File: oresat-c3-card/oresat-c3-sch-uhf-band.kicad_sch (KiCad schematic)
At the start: 124 parts, among them Q3 DMP2035UQ-7, Q4 DMN3028LQ-7, U18 LT5534, U19 BDCN-20-13+, U20 QPC1022, U21 TQP7M9105, U22 LT5534, U25 SN74LVC1G11IDCKRQ1, U26 TLV7041DBV, U27 SN74LVC1G04DCKR, U29 TQP3M9036, U32 SF2446E, U33 SF2446E, U40 MAX941EUA+, U44 AT86RF215, U45 NCS2-62+, U47 QPC1022, X3 TXETALSANF-26.000000

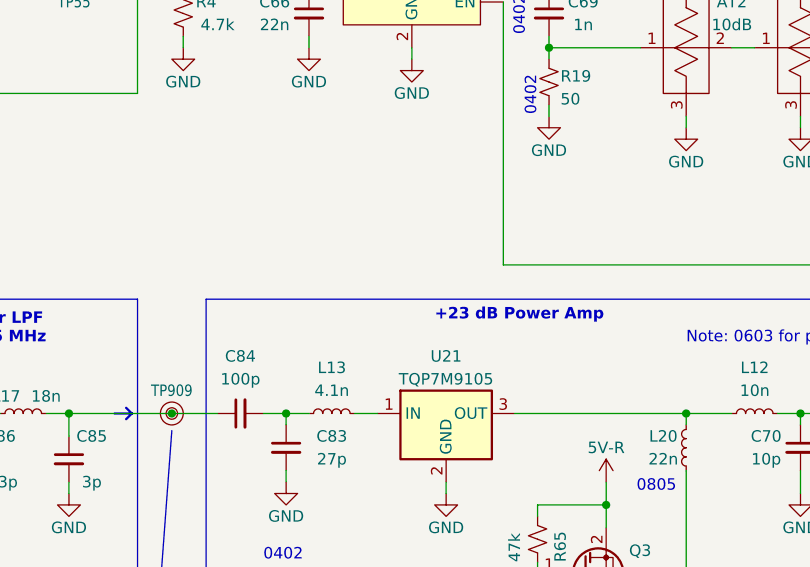
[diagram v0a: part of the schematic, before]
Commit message: All DRC exclusing RF traces are cleaned up.  RF traces cleaned up with mask and bends. Some more notes in the schematic for future us.
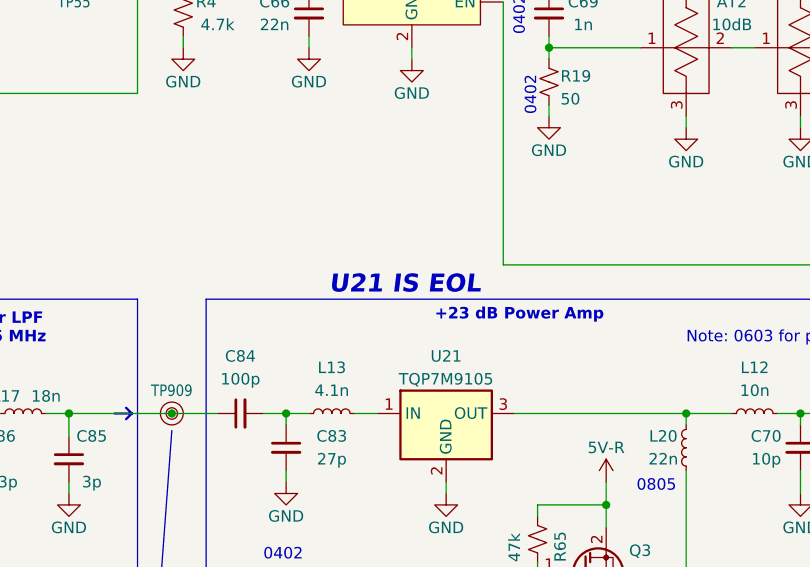
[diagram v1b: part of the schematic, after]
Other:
- note added: "U21 IS EOL"
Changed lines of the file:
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@@
+		)
+	)
+	(text "U21 IS EOL"
+		(exclude_from_sim no)
+		(at 251.968 86.106 0)
+		(effects
+			(font
+				(face "KiCad Font")
+				(size 2 2)
+				(thickness 0.254)
+				(bold yes)
+				(italic yes)
+				(color 255 0 33 1)
+			)
 		)
 	)

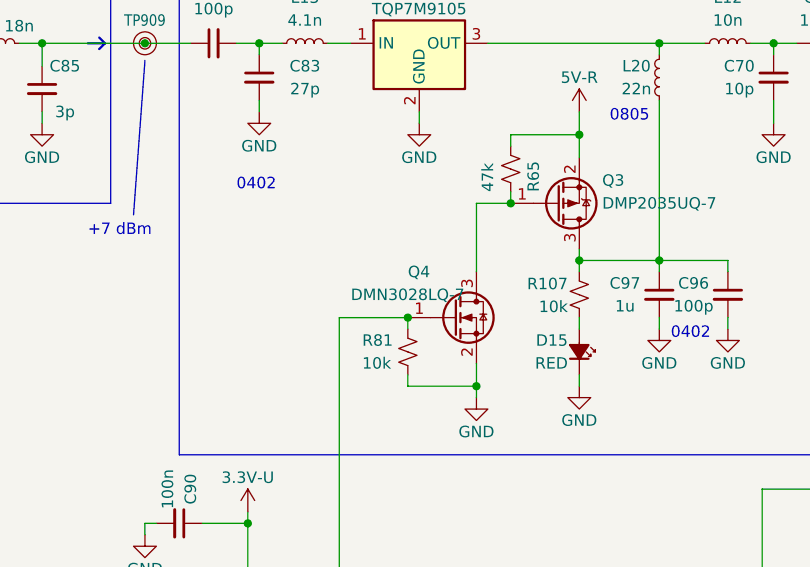
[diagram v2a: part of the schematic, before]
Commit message: Last minute fixes.
Added Theo's space buzzer. Added important kaomoji message. Fixed Makefile so that it ignores
bad VRML footprints. Successfully builds!
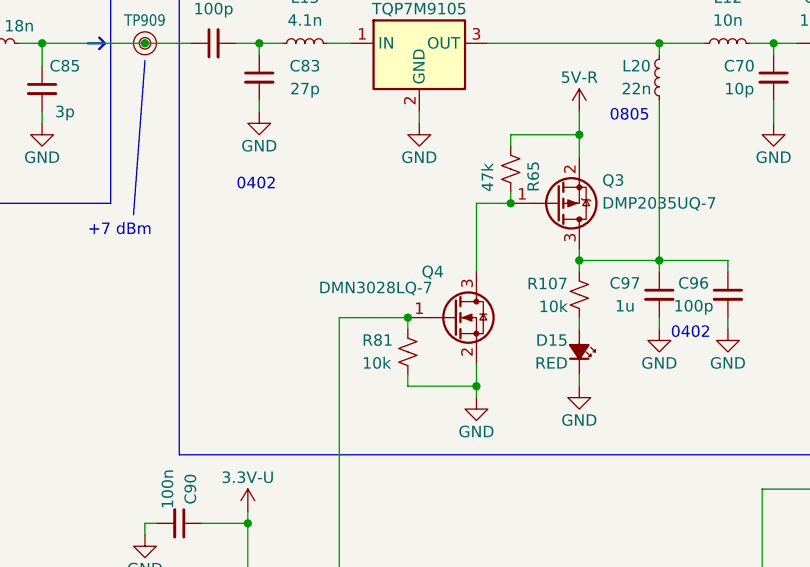
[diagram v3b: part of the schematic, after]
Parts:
- AT1, AT2, AT3, AT4: DST Digi-Key -> DigiKey
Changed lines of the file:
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@@
 			)
 		)
-		(property "DST" "Digi-Key"
+		(property "DST" "DigiKey"
 			(at 283.21 59.69 0)
 			(effects
@@
 		(dnp no)
 		(property "Reference" "Q4"
-			(at 255.27 125.73 0)
+			(at 256.794 125.73 0)
 			(effects
 				(font
@@
 		)
 		(property "Value" "DMN3028LQ-7"
-			(at 248.92 128.27 0)
+			(at 245.364 127.508 0)
 			(effects
 				(font
@@
 			)
 		)
-		(property "DST" "Digi-Key"
+		(property "DST" "DigiKey"
 			(at 308.61 59.69 0)
 			(effects
@@
 			)
 		)
-		(property "DST" "Digi-Key"
+		(property "DST" "DigiKey"
 			(at 345.44 59.69 0)
 			(effects
@@
 			)
 		)
-		(property "DST" "Digi-Key"
+		(property "DST" "DigiKey"
 			(at 295.91 59.69 0)
 			(effects

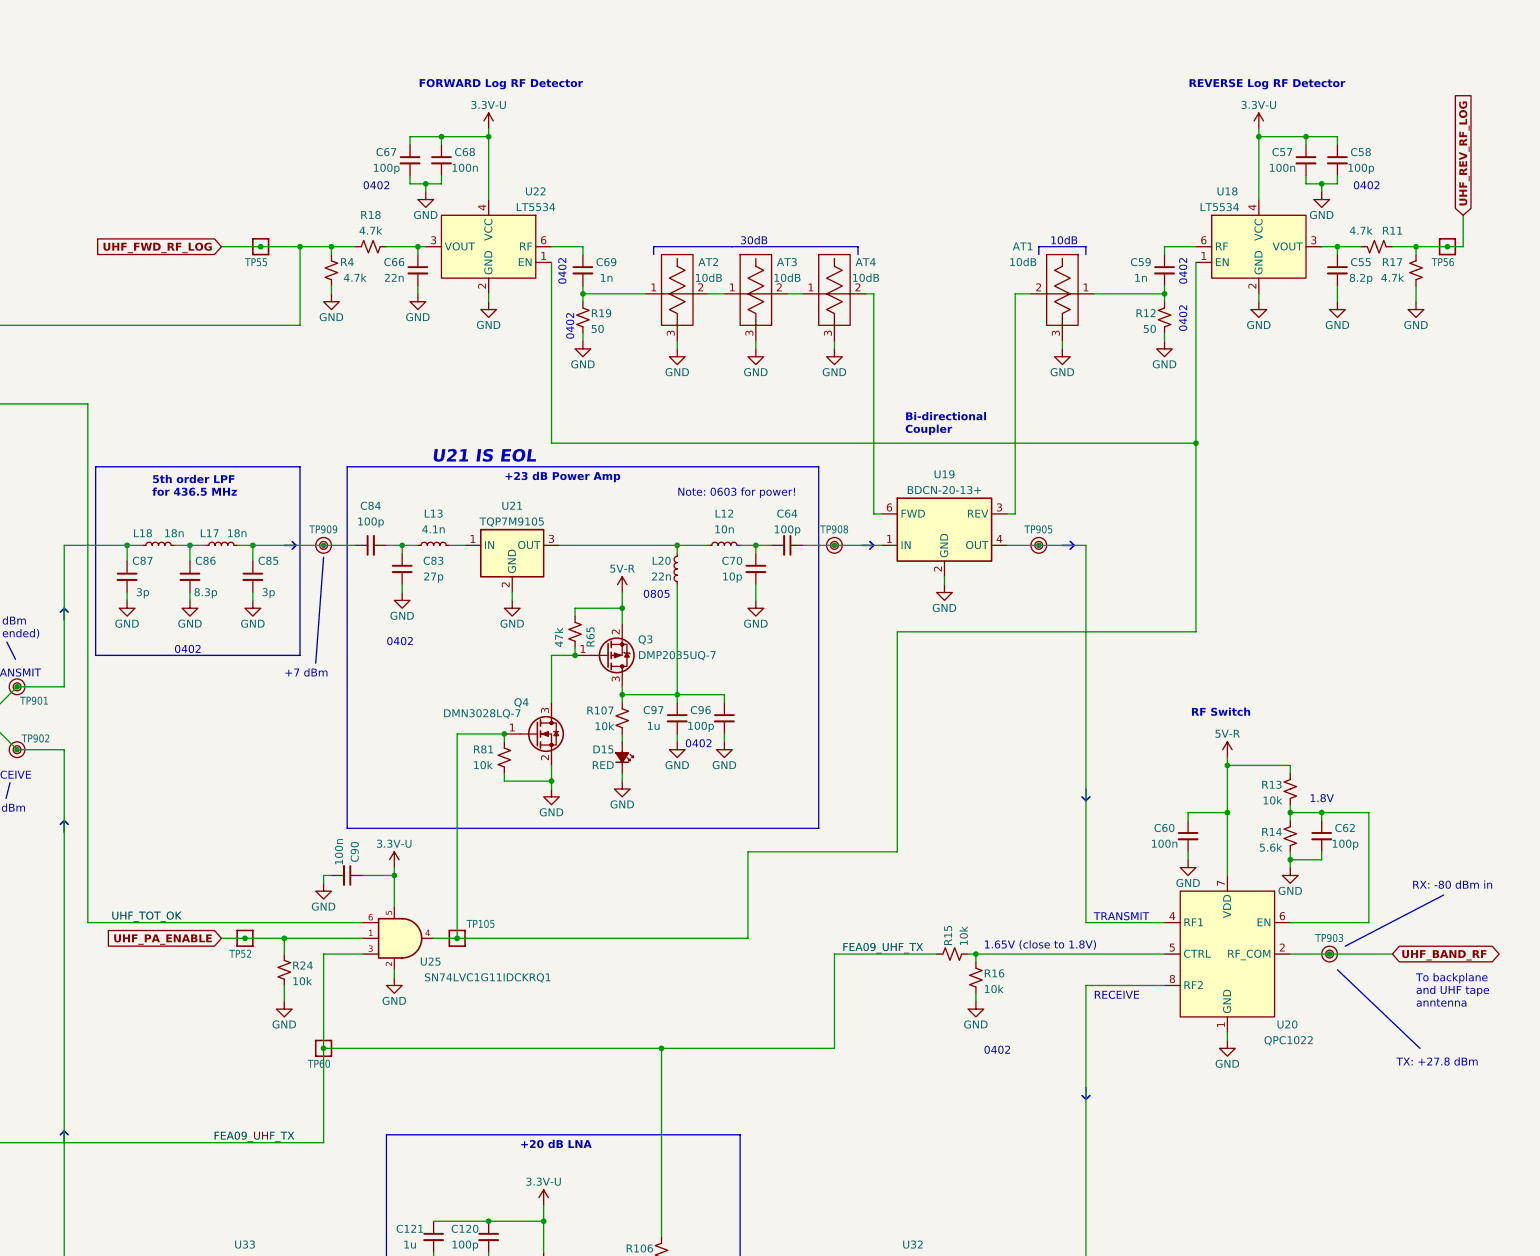
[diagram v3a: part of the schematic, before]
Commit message: Minor polishing on schematic, mostly text notes.
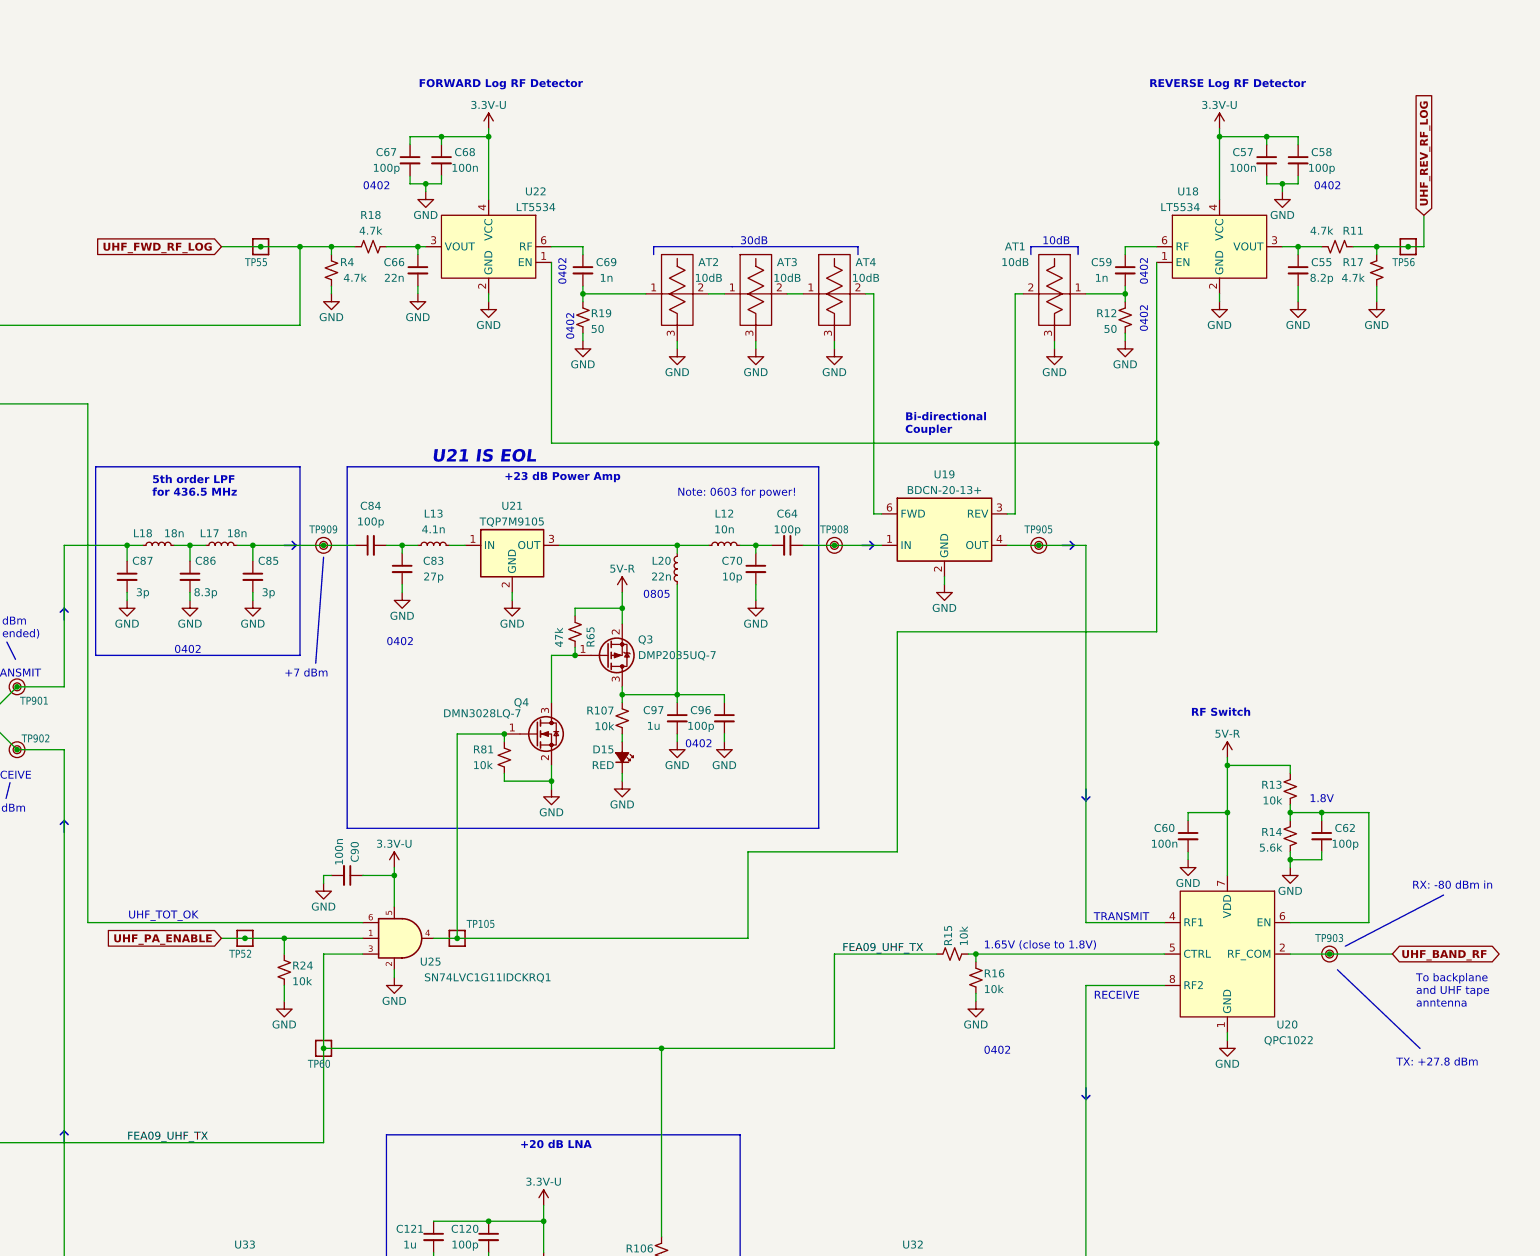
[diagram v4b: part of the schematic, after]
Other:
- note added: "UHF_TOT_OK"
- moved on the sheet: AT1, C55, C57, C58, C59, R11, R12, R17, TP56, U18

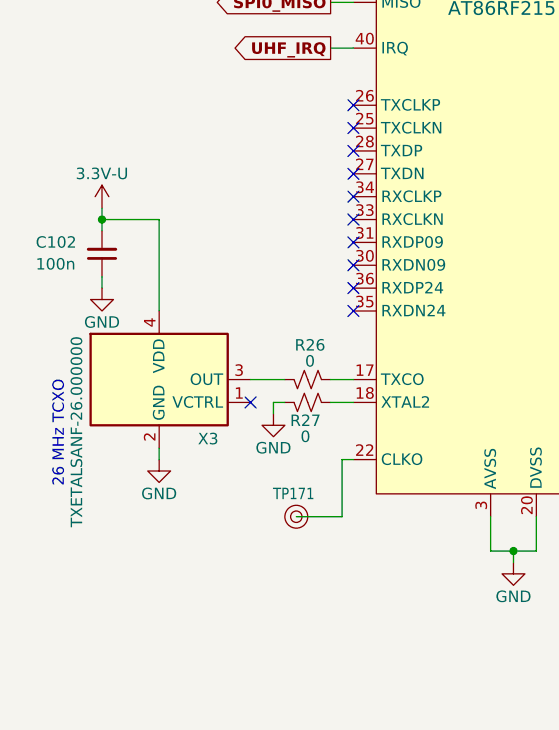
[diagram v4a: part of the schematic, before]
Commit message: Fixed a test point, cleaned up silk screen, and moved date up to today.
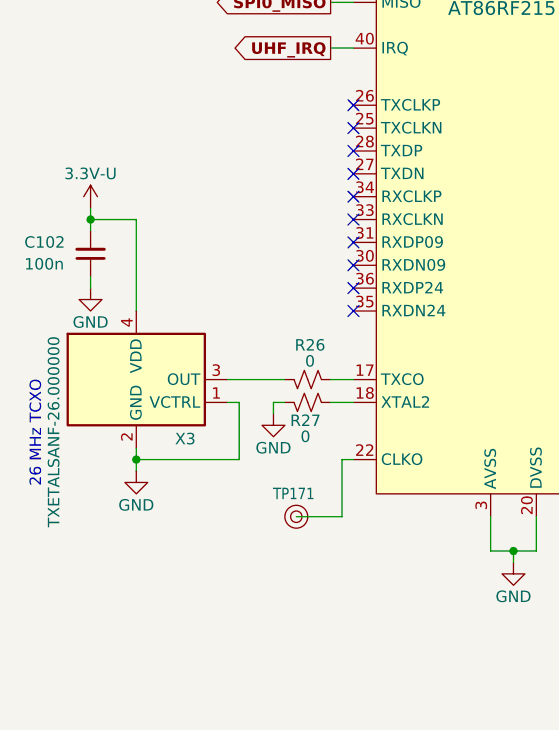
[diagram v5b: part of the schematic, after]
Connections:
- net GND: now also X3.1 (VCTRL)
- no-connect marks 15 -> 14
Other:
- moved on the sheet: C102, X3
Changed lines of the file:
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@@
 	(title_block
 		(title "OreSat C3 Card")
-		(date "2026-03-17")
+		(date "2026-03-20")
 		(rev "7.0")
 		(company "Portland State Aerospace Society")
@@
 	(text "26 MHz TCXO"
 		(exclude_from_sim no)
-		(at 16.764 166.116 90)
+		(at 14.224 166.116 90)
 		(effects
 			(font
@@
 	)
 	(junction
-		(at 21.59 142.24)
+		(at 20.32 142.24)
 		(diameter 0)
 		(color 0 0 0 0)
@@
 	)
 	(junction
+		(at 25.4 168.91)
+		(diameter 0)
+		(color 0 0 0 0)
+	)
+	(junction
 		(at 55.88 236.22)
 		(diameter 0)
@@
 	)
 	(no_connect
-		(at 38.1 162.56)
-	)
-	(no_connect
 		(at 49.53 134.62)
 	)
@@
 	(wire
 		(pts
-			(xy 21.59 140.97) (xy 21.59 142.24)
+			(xy 20.32 140.97) (xy 20.32 142.24)
 		)
 		(stroke
@@
 	(wire
 		(pts
+			(xy 25.4 168.91) (xy 25.4 170.18)
+		)
+		(stroke
+			(width 0)
+			(type default)
+		)
+	)
+	(wire
+		(pts
 			(xy 382.27 135.89) (xy 382.27 137.16)
 		)
@@
 	(wire
 		(pts
-			(xy 27.94 152.4) (xy 27.94 142.24)
+			(xy 25.4 152.4) (xy 25.4 142.24)
 		)
 		(stroke
@@
 	(wire
 		(pts
-			(xy 21.59 148.59) (xy 21.59 149.86)
+			(xy 20.32 148.59) (xy 20.32 149.86)
 		)
 		(stroke
@@
 		)
 	)
+	(wire
+		(pts
+			(xy 36.83 168.91) (xy 25.4 168.91)
+		)
+		(stroke
+			(width 0)
+			(type default)
+		)
+	)
 	(polyline
 		(pts
@@
 	(wire
 		(pts
-			(xy 21.59 142.24) (xy 21.59 143.51)
+			(xy 20.32 142.24) (xy 20.32 143.51)
 		)
 		(stroke
@@
 	(wire
 		(pts
+			(xy 36.83 162.56) (xy 35.56 162.56)
+		)
+		(stroke
+			(width 0)
+			(type default)
+		)
+	)
+	(wire
+		(pts
 			(xy 140.97 93.98) (xy 140.97 95.25)
 		)
@@
 	(wire
 		(pts
-			(xy 27.94 167.64) (xy 27.94 168.91)
+			(xy 25.4 167.64) (xy 25.4 168.91)
 		)
 		(stroke
@@
 	(wire
 		(pts
-			(xy 38.1 160.02) (xy 41.91 160.02)
+			(xy 35.56 160.02) (xy 41.91 160.02)
 		)
 		(stroke
@@
 	(wire
 		(pts
-			(xy 21.59 142.24) (xy 27.94 142.24)
+			(xy 20.32 142.24) (xy 25.4 142.24)
 		)
 		(stroke
@@
 	(wire
 		(pts
+			(xy 36.83 162.56) (xy 36.83 168.91)
+		)
+		(stroke
+			(width 0)
+			(type default)
+		)
+	)
+	(wire
+		(pts
 			(xy 91.44 160.02) (xy 91.44 161.29)
 		)
@@
 	(symbol
 		(lib_id "power:GND")
-		(at 27.94 168.91 0)
+		(at 25.4 170.18 0)
 		(unit 1)
 		(exclude_from_sim no)
@@
 		(dnp no)
 		(property "Reference" "#PWR025"
-			(at 27.94 175.26 0)
+			(at 25.4 176.53 0)
 			(effects
 				(font
@@
 		)
 		(property "Value" "GND"
-			(at 27.94 172.72 0)
+			(at 25.4 173.99 0)
 			(effects
 				(font
@@
 		)
 		(property "Footprint" ""
-			(at 27.94 168.91 0)
+			(at 25.4 170.18 0)
 			(effects
 				(font
@@
 		)
 		(property "Datasheet" ""
-			(at 27.94 168.91 0)
+			(at 25.4 170.18 0)
 			(effects
 				(font
@@
 		)
 		(property "Description" "Power symbol creates a global label with name \"GND\" , ground"
-			(at 27.94 168.91 0)
+			(at 25.4 170.18 0)
 			(effects
 				(font
@@
 	(symbol
 		(lib_id "power:GND")
-		(at 21.59 149.86 0)
+		(at 20.32 149.86 0)
 		(unit 1)
 		(exclude_from_sim no)
@@
 		(dnp no)
 		(property "Reference" "#PWR024"
-			(at 21.59 156.21 0)
+			(at 20.32 156.21 0)
 			(effects
 				(font
@@
 		)
 		(property "Value" "GND"
-			(at 21.59 153.67 0)
+			(at 20.32 153.67 0)
 			(effects
 				(font
@@
 		)
 		(property "Footprint" ""
-			(at 21.59 149.86 0)
+			(at 20.32 149.86 0)
 			(effects
 				(font
@@
 		)
 		(property "Datasheet" ""
-			(at 21.59 149.86 0)
+			(at 20.32 149.86 0)
 			(effects
 				(font
@@
 		)
 		(property "Description" "Power symbol creates a global label with name \"GND\" , ground"
-			(at 21.59 149.86 0)
+			(at 20.32 149.86 0)
 			(effects
 				(font
@@
 	(symbol
 		(lib_id "oresat-ics:Taiten-TY-Series-TXCO")
-		(at 27.94 160.02 0)
+		(at 25.4 160.02 0)
 		(unit 1)
 		(exclude_from_sim no)
@@
 		(dnp no)
 		(property "Reference" "X3"
-			(at 34.544 166.624 0)
+			(at 32.004 166.624 0)
 			(effects
 				(font
@@
 		)
 		(property "Value" "TXETALSANF-26.000000"
-			(at 18.796 155.194 90)
+			(at 16.256 155.194 90)
 			(effects
 				(font
@@
 		)
 		(property "Footprint" "oresat-ics:X_TCXO_SMD_Taitien_2.5x2.0mm"
-			(at 27.94 139.7 0)
+			(at 25.4 139.7 0)
 			(effects
 				(font
@@
 		)
 		(property "Datasheet" "https://www.taitien.com/wp-content/uploads/2015/12/XO-0081_TY.pdf"
-			(at 27.94 137.16 0)
+			(at 25.4 137.16 0)
 			(effects
 				(font
@@
 		)
 		(property "Description" "26 MHz TCXO Clipped Sine Wave Oscillator 2.8V ~ 3.3V 4-SMD, No Lead"
-			(at 27.94 160.02 0)
+			(at 25.4 160.02 0)
 			(effects
 				(font
@@
 		)
 		(property "DIS" "DigiKey"
-			(at 27.94 160.02 0)
+			(at 25.4 160.02 0)
 			(effects
 				(font
@@
 		)
 		(property "DPN" "1664-TXETALSANF-26.000000CT-ND"
-			(at 27.94 160.02 0)
+			(at 25.4 160.02 0)
 			(effects
 				(font
@@
 		)
 		(property "MFR" "Taitien"
-			(at 27.94 160.02 0)
+			(at 25.4 160.02 0)
 			(effects
 				(font
@@
 		)
 		(property "MPN" "TXETALSANF-26.000000"
-			(at 27.94 160.02 0)
+			(at 25.4 160.02 0)
 			(effects
 				(font
@@
 		)
 		(property "DST" "DigiKey"
-			(at 27.94 160.02 0)
+			(at 25.4 160.02 0)
 			(effects
 				(font
@@
 	(symbol
 		(lib_id "oresat-power:3.3V-U")
-		(at 21.59 140.97 0)
+		(at 20.32 140.97 0)
 		(unit 1)
 		(exclude_from_sim no)
@@
 		(fields_autoplaced yes)
 		(property "Reference" "#3V3-U023"
-			(at 21.59 144.78 0)
+			(at 20.32 144.78 0)
 			(effects
 				(font
@@
 		)
 		(property "Value" "3.3V-U"
-			(at 21.59 137.16 0)
+			(at 20.32 137.16 0)
 			(effects
 				(font
@@
 		)
 		(property "Footprint" ""
-			(at 21.59 140.97 0)
+			(at 20.32 140.97 0)
 			(effects
 				(font
@@
 		)
 		(property "Datasheet" ""
-			(at 21.59 140.97 0)
+			(at 20.32 140.97 0)
 			(effects
 				(font
@@
 		)
 		(property "Description" ""
-			(at 21.59 140.97 0)
+			(at 20.32 140.97 0)
 			(effects
 				(font
@@
 	(symbol
 		(lib_id "Device:C_Small")
-		(at 21.59 146.05 180)
+		(at 20.32 146.05 180)
 		(unit 1)
 		(exclude_from_sim no)
@@
 		(dnp no)
 		(property "Reference" "C102"
-			(at 14.224 144.78 0)
+			(at 12.954 144.78 0)
 			(effects
 				(font
@@
 		)
 		(property "Value" "100n"
-			(at 14.224 147.2043 0)
+			(at 12.954 147.2043 0)
 			(effects
 				(font
@@
 		)
 		(property "Footprint" "oresat-passives:0603-C-NOSILK"
-			(at 21.59 146.05 0)
+			(at 20.32 146.05 0)
 			(effects
 				(font
@@
 		)
 		(property "Datasheet" "https://search.kemet.com/download/specsheet/C0603C104K5RACAUTO"
-			(at 21.59 146.05 0)
+			(at 20.32 146.05 0)
 			(effects
 				(font
@@
 		)
 		(property "Description" "0.1 µF ±10% 50V Ceramic Capacitor X7R 0603 (1608 Metric)"
-			(at 21.59 146.05 0)
+			(at 20.32 146.05 0)
 			(effects
 				(font
@@
 		)
 		(property "DIS" "DigiKey"
-			(at 21.59 146.05 0)
+			(at 20.32 146.05 0)
 			(effects
 				(font
@@
 		)
 		(property "DPN" "399-6856-1-ND"
-			(at 21.59 146.05 0)
+			(at 20.32 146.05 0)
 			(effects
 				(font
@@
 		)
 		(property "MFR" "KEMET"
-			(at 21.59 146.05 0)
+			(at 20.32 146.05 0)
 			(effects
 				(font
@@
 		)
 		(property "MPN" "C0603C104K5RACAUTO"
-			(at 21.59 146.05 0)
+			(at 20.32 146.05 0)
 			(effects
 				(font
@@
 		)
 		(property "DST" "DigiKey"
-			(at 21.59 146.05 0)
+			(at 20.32 146.05 0)
 			(effects
 				(font
